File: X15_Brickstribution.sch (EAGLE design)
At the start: 87 parts, among them J1 IPL1-104-01-X-S-K, Q1 310mA/60V/1.6Ω, U5 IC_L4970A, U6 DIODE_STPS1545CT, U7 IC_L4970A, U8 DIODE_STPS1545CT

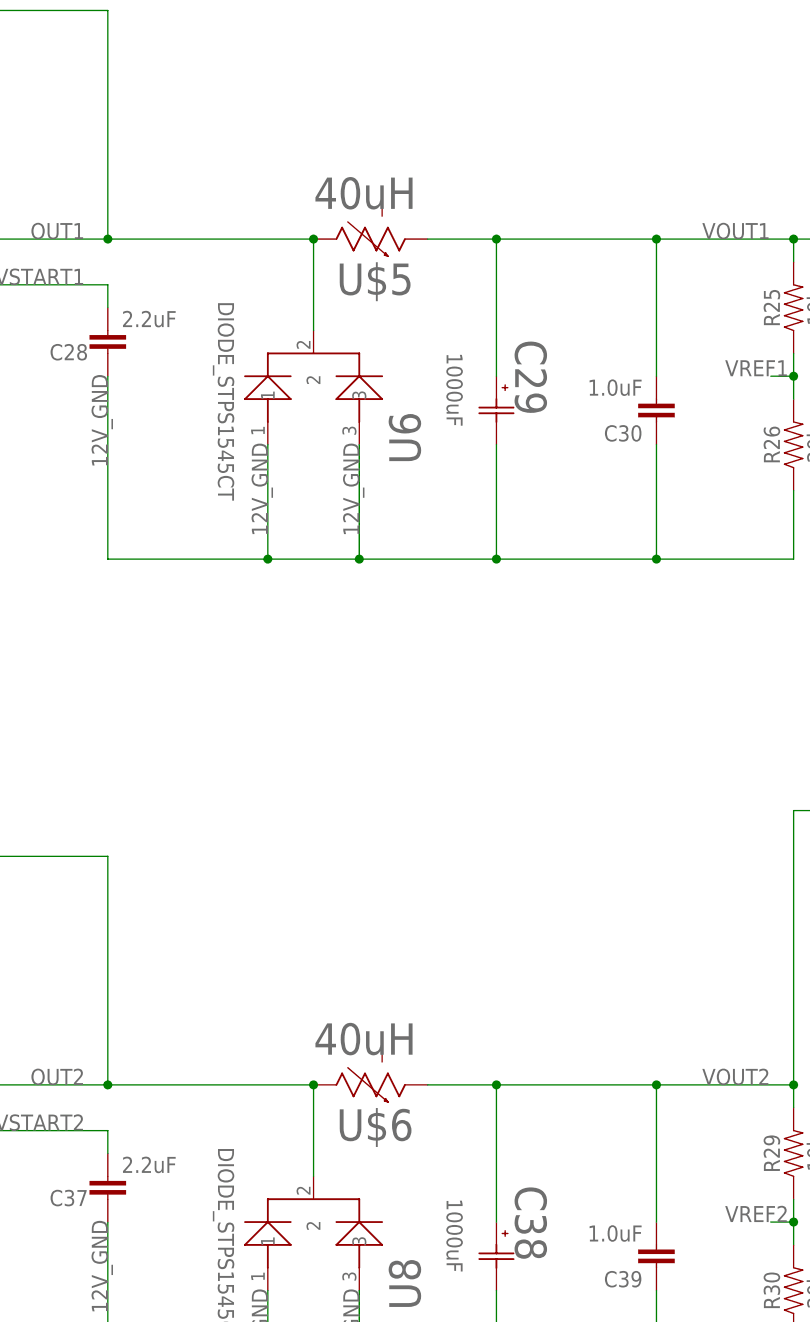
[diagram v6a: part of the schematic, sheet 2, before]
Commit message: Changed inductor out and reconfigured traces.
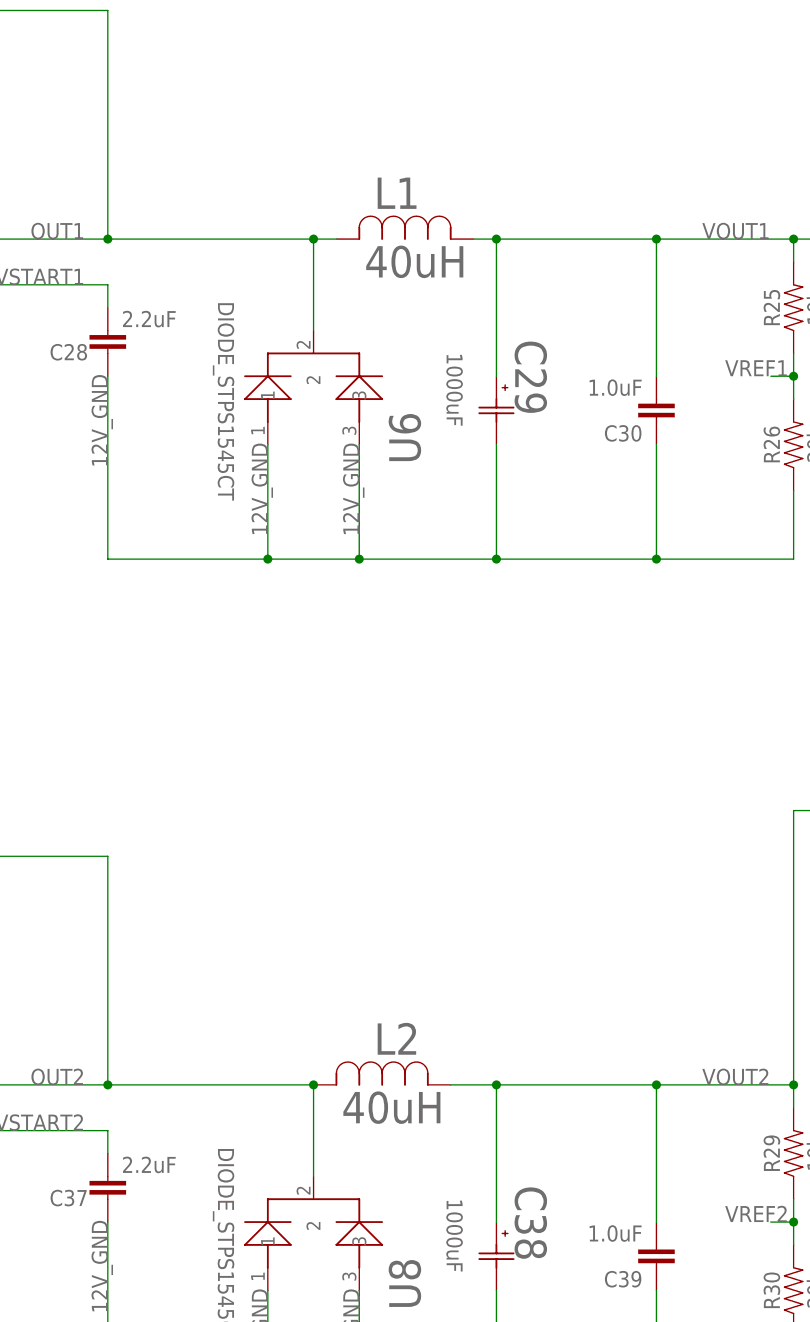
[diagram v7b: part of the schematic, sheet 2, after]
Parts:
- removed U$5, U$6: 40uH, X15_Brickstribution:IND_PG1096_26X26_PUL-M
- added L1, L2: 40uH, X15_Brickstribution:IND_2308-V-RC
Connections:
- net OUT1: now also L1.2; no longer U$5.2
- net OUT2: now also L2.2; no longer U$6.2
- net VOUT1: now also L1.1; no longer U$5.1
- net VOUT2: now also L2.1; no longer U$6.1
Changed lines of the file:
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@@
 <part name="C28" library="SparkFun-Capacitors" library_urn="urn:adsk.eagle:library:510" deviceset="2.2UF" device="-0603-10V-20%" package3d_urn="urn:adsk.eagle:package:37414/1" value="2.2uF"/>
 <part name="C29" library="X15_Brickstribution" deviceset="CAP_PCG1A102MCL1GS" device="CAP_PC_10X12P7_NCH-M" value="1000uF"/>
-<part name="U$5" library="X15_Brickstribution" deviceset="IND_PG1096_26X26_PUL-M" device="" value="40uH"/>
 <part name="C30" library="SparkFun-Capacitors" library_urn="urn:adsk.eagle:library:510" deviceset="1.0UF" device="-0603-16V-10%" package3d_urn="urn:adsk.eagle:package:37414/1" value="1.0uF"/>
 <part name="R25" library="SparkFun-Resistors" library_urn="urn:adsk.eagle:library:532" deviceset="10KOHM" device="-0603-1/10W-1%" package3d_urn="urn:adsk.eagle:package:39650/1" value="10k"/>
@@
 <part name="C37" library="SparkFun-Capacitors" library_urn="urn:adsk.eagle:library:510" deviceset="2.2UF" device="-0603-10V-20%" package3d_urn="urn:adsk.eagle:package:37414/1" value="2.2uF"/>
 <part name="C38" library="X15_Brickstribution" deviceset="CAP_PCG1A102MCL1GS" device="CAP_PC_10X12P7_NCH-M" value="1000uF"/>
-<part name="U$6" library="X15_Brickstribution" deviceset="IND_PG1096_26X26_PUL-M" device="" value="40uH"/>
 <part name="C39" library="SparkFun-Capacitors" library_urn="urn:adsk.eagle:library:510" deviceset="1.0UF" device="-0603-16V-10%" package3d_urn="urn:adsk.eagle:package:37414/1" value="1.0uF"/>
 <part name="R29" library="SparkFun-Resistors" library_urn="urn:adsk.eagle:library:532" deviceset="10KOHM" device="-0603-1/10W-1%" package3d_urn="urn:adsk.eagle:package:39650/1" value="10k"/>
@@
 <part name="H4" library="X15_Brickstribution" deviceset="6-32-HOLE" device="" package3d_urn="urn:adsk.eagle:package:24384748/2"/>
 <part name="J1" library="X15_Brickstribution" deviceset="IPL1-104-01-X-S-K" device=""/>
+<part name="L2" library="X15_Brickstribution" deviceset="IND_2308-V-RC" device="" value="40uH"/>
+<part name="L1" library="X15_Brickstribution" deviceset="IND_2308-V-RC" device="" value="40uH"/>
 </parts>
 <sheets>
@@
 <attribute name="NAME" x="192.5828" y="189.5094" size="3.4798" layer="95" ratio="10" rot="SR270"/>
 </instance>
-<instance part="U$5" gate="G$1" x="170.18" y="200.66" smashed="yes" rot="R270">
-<attribute name="NAME" x="172.72" y="194.4624" size="3.4798" layer="95" ratio="10" rot="SR0"/>
-<attribute name="VALUE" x="170.18" y="204.0128" size="3.4798" layer="96" ratio="10" rot="SR0"/>
-</instance>
 <instance part="C30" gate="G$1" x="208.28" y="182.88" smashed="yes" rot="R180">
 <attribute name="NAME" x="206.756" y="179.959" size="1.778" layer="95" font="vector" rot="R180"/>
@@
 <attribute name="NAME" x="192.5828" y="95.5294" size="3.4798" layer="95" ratio="10" rot="SR270"/>
 </instance>
-<instance part="U$6" gate="G$1" x="170.18" y="106.68" smashed="yes" rot="R270">
-<attribute name="NAME" x="172.72" y="100.4824" size="3.4798" layer="95" ratio="10" rot="SR0"/>
-<attribute name="VALUE" x="170.18" y="110.0328" size="3.4798" layer="96" ratio="10" rot="SR0"/>
-</instance>
 <instance part="C39" gate="G$1" x="208.28" y="88.9" smashed="yes" rot="R180">
 <attribute name="NAME" x="206.756" y="85.979" size="1.778" layer="95" font="vector" rot="R180"/>
@@
 <attribute name="NAME" x="281.44" y="144.78" size="1.778" layer="95"/>
 <attribute name="VALUE" x="281.94" y="129.54" size="1.778" layer="96"/>
+</instance>
+<instance part="L2" gate="A" x="170.18" y="106.68" smashed="yes">
+<attribute name="VALUE" x="173.2788" y="102.4128" size="3.4798" layer="96" ratio="10" rot="SR0"/>
+<attribute name="NAME" x="176.8856" y="110.0328" size="3.4798" layer="95" ratio="10" rot="SR0"/>
+</instance>
+<instance part="L1" gate="A" x="172.72" y="200.66" smashed="yes">
+<attribute name="VALUE" x="175.8188" y="196.3928" size="3.4798" layer="96" ratio="10" rot="SR0"/>
+<attribute name="NAME" x="176.8856" y="204.0128" size="3.4798" layer="95" ratio="10" rot="SR0"/>
 </instance>
 </instances>
@@
 <junction x="147.32" y="106.68"/>
 <pinref part="C31" gate="G$1" pin="2"/>
-<pinref part="U$6" gate="G$1" pin="2"/>
+<pinref part="L2" gate="A" pin="2"/>
 <junction x="170.18" y="106.68"/>
 </segment>
@@
 <net name="VOUT2" class="0">
 <segment>
-<pinref part="U$6" gate="G$1" pin="1"/>
 <pinref part="C38" gate="A" pin="1"/>
-<wire x1="182.88" y1="106.68" x2="190.5" y2="106.68" width="0.1524" layer="91"/>
 <wire x1="190.5" y1="106.68" x2="190.5" y2="91.44" width="0.1524" layer="91"/>
 <pinref part="C39" gate="G$1" pin="2"/>
 <wire x1="190.5" y1="106.68" x2="208.28" y2="106.68" width="0.1524" layer="91"/>
 <wire x1="208.28" y1="106.68" x2="208.28" y2="91.44" width="0.1524" layer="91"/>
-<junction x="190.5" y="106.68"/>
 <wire x1="208.28" y1="106.68" x2="223.52" y2="106.68" width="0.1524" layer="91"/>
 <junction x="208.28" y="106.68"/>
@@
 <wire x1="223.52" y1="137.16" x2="243.84" y2="137.16" width="0.1524" layer="91"/>
 <junction x="223.52" y="106.68"/>
+<pinref part="L2" gate="A" pin="1"/>
+<wire x1="185.42" y1="106.68" x2="190.5" y2="106.68" width="0.1524" layer="91"/>
+<junction x="190.5" y="106.68"/>
 </segment>
 </net>
@@
 <net name="VOUT1" class="0">
 <segment>
-<pinref part="U$5" gate="G$1" pin="1"/>
 <pinref part="C29" gate="A" pin="1"/>
-<wire x1="182.88" y1="200.66" x2="190.5" y2="200.66" width="0.1524" layer="91"/>
 <wire x1="190.5" y1="200.66" x2="190.5" y2="185.42" width="0.1524" layer="91"/>
 <pinref part="C30" gate="G$1" pin="2"/>
 <wire x1="190.5" y1="200.66" x2="208.28" y2="200.66" width="0.1524" layer="91"/>
 <wire x1="208.28" y1="200.66" x2="208.28" y2="185.42" width="0.1524" layer="91"/>
-<junction x="190.5" y="200.66"/>
 <wire x1="208.28" y1="200.66" x2="223.52" y2="200.66" width="0.1524" layer="91"/>
 <junction x="208.28" y="200.66"/>
@@
 <pinref part="R31" gate="A" pin="3"/>
 <wire x1="236.22" y1="142.24" x2="243.84" y2="142.24" width="0.1524" layer="91"/>
+<pinref part="L1" gate="A" pin="1"/>
+<wire x1="187.96" y1="200.66" x2="190.5" y2="200.66" width="0.1524" layer="91"/>
+<junction x="190.5" y="200.66"/>
 </segment>
 </net>
@@
 <junction x="147.32" y="200.66"/>
 <pinref part="C22" gate="G$1" pin="2"/>
-<pinref part="U$5" gate="G$1" pin="2"/>
+<pinref part="L1" gate="A" pin="2"/>
+<wire x1="170.18" y1="200.66" x2="172.72" y2="200.66" width="0.1524" layer="91"/>
 <junction x="170.18" y="200.66"/>
 </segment>

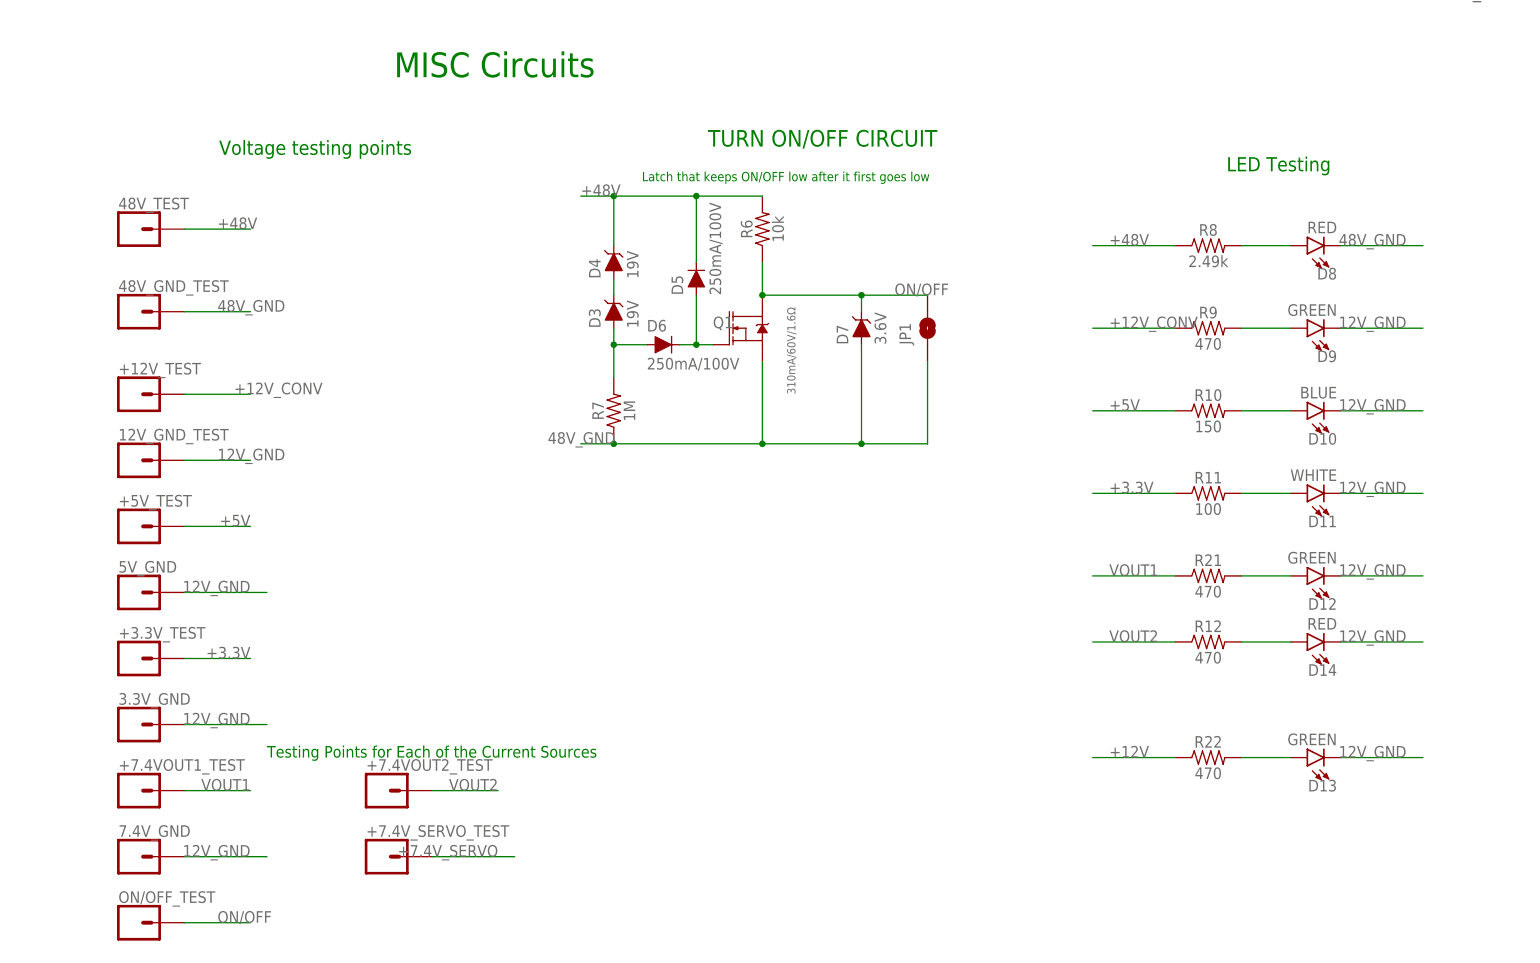
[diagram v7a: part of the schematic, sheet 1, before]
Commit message: Changed polygons and connections to reference voltage
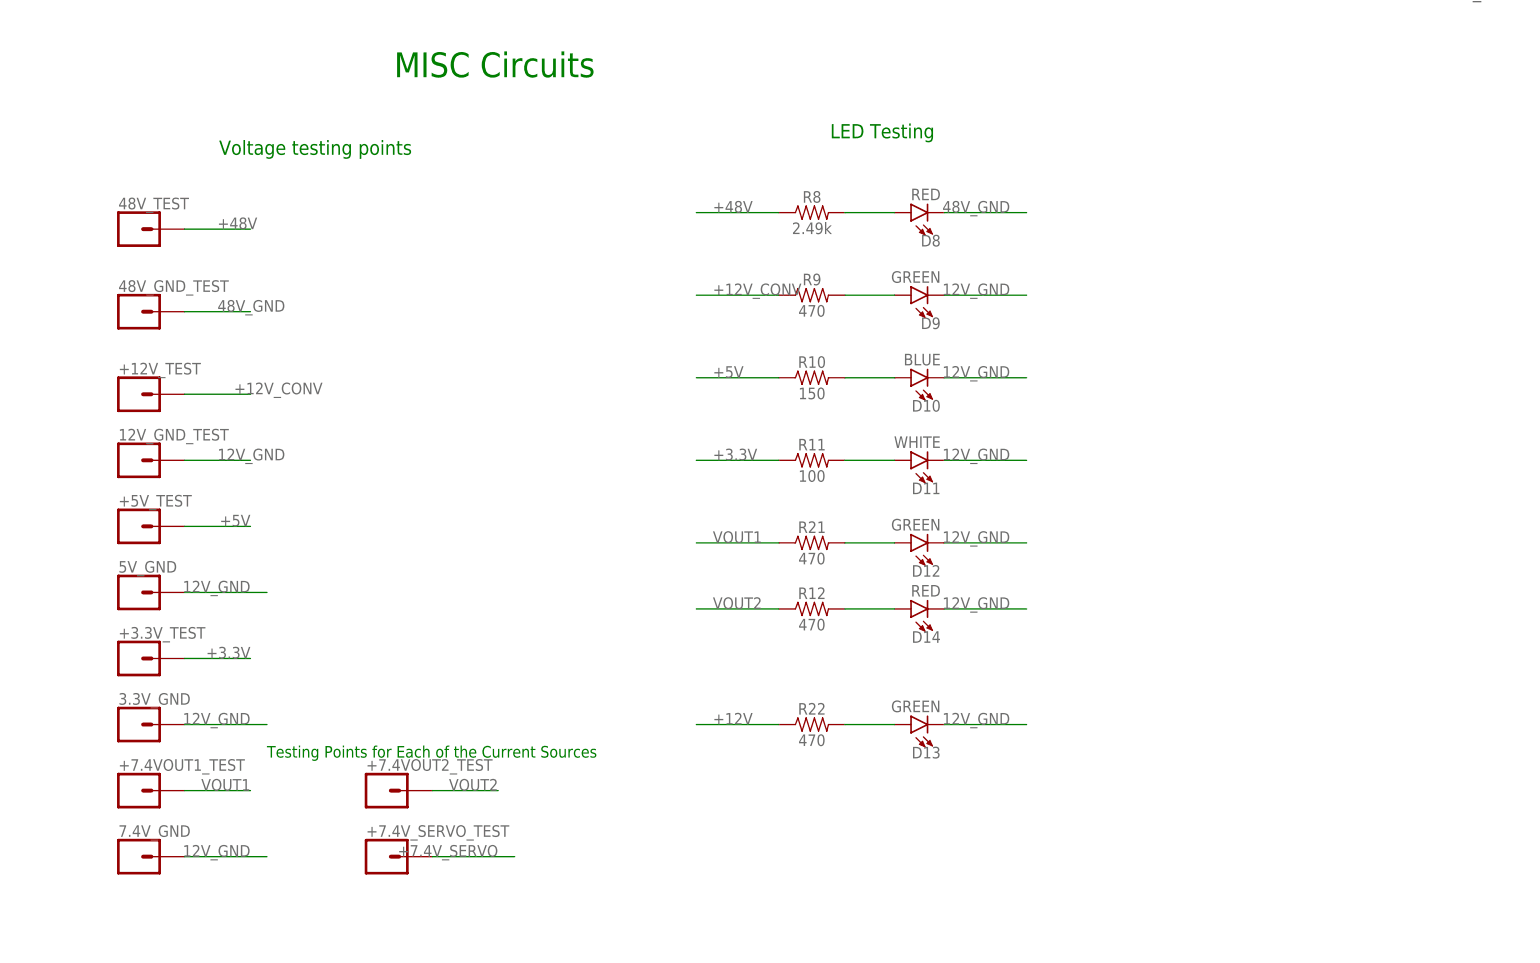
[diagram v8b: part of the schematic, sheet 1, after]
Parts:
- removed D3, D4: 19V, SparkFun-DiscreteSemi:DIODE-ZENER-BZT52C3V6S
- removed D5, D6: 250mA/100V, SparkFun-DiscreteSemi:DIODE-BAS16J
- removed D7: 3.6V, SparkFun-DiscreteSemi:DIODE-ZENER-BZT52C3V6S
- removed JP1: JUMPER-SMT_2_NO_SILK_ROUND, SparkFun-Jumpers:JUMPER-SMT_2_NO_SILK_ROUND
- removed ON/OFF_TEST: (no value), SparkFun-Connectors:CONN_01
- removed Q1: 310mA/60V/1.6Ω, SparkFun-DiscreteSemi:MOSFET-NCH-2N7002PW
- removed R6: 10k, SparkFun-Resistors:10KOHM-0603-1/10W-1%
- removed R7: 1M, SparkFun-Resistors:1MOHM-0603-1/4W-5%
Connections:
- removed net N$5: D3.C, D4.A
- removed net N$6: D3.A, D6.A, R7.2
- removed net N$7: D5.A, D6.C, Q1.G
- removed net ON/OFF: D7.C, JP1.2, ON/OFF_TEST.1, Q1.D, R6.1
- net +48V: no longer D4.C, D5.C, R6.2
- net 48V_GND: no longer D7.A, JP1.1, Q1.S, R7.1
- net OUT1: now also R25.2
- net OUT2: now also R29.2
- net VOUT1: no longer R25.2
- net VOUT2: no longer R29.2
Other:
- note removed: "Latch that keeps ON/OFF low after it first goes low"
- note removed: "TURN ON/OFF CIRCUIT"
- moved on the sheet: C29, C30, C38, C39, D10, D11, D12, D13, D14, D8, D9, L1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
